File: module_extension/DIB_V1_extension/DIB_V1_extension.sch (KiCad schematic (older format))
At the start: 12 parts, among them J1 20-pin power socket, J3 28-pin module socket, J3 PROBE, J4 CABLE, J5 PROBE, J6 CABLE

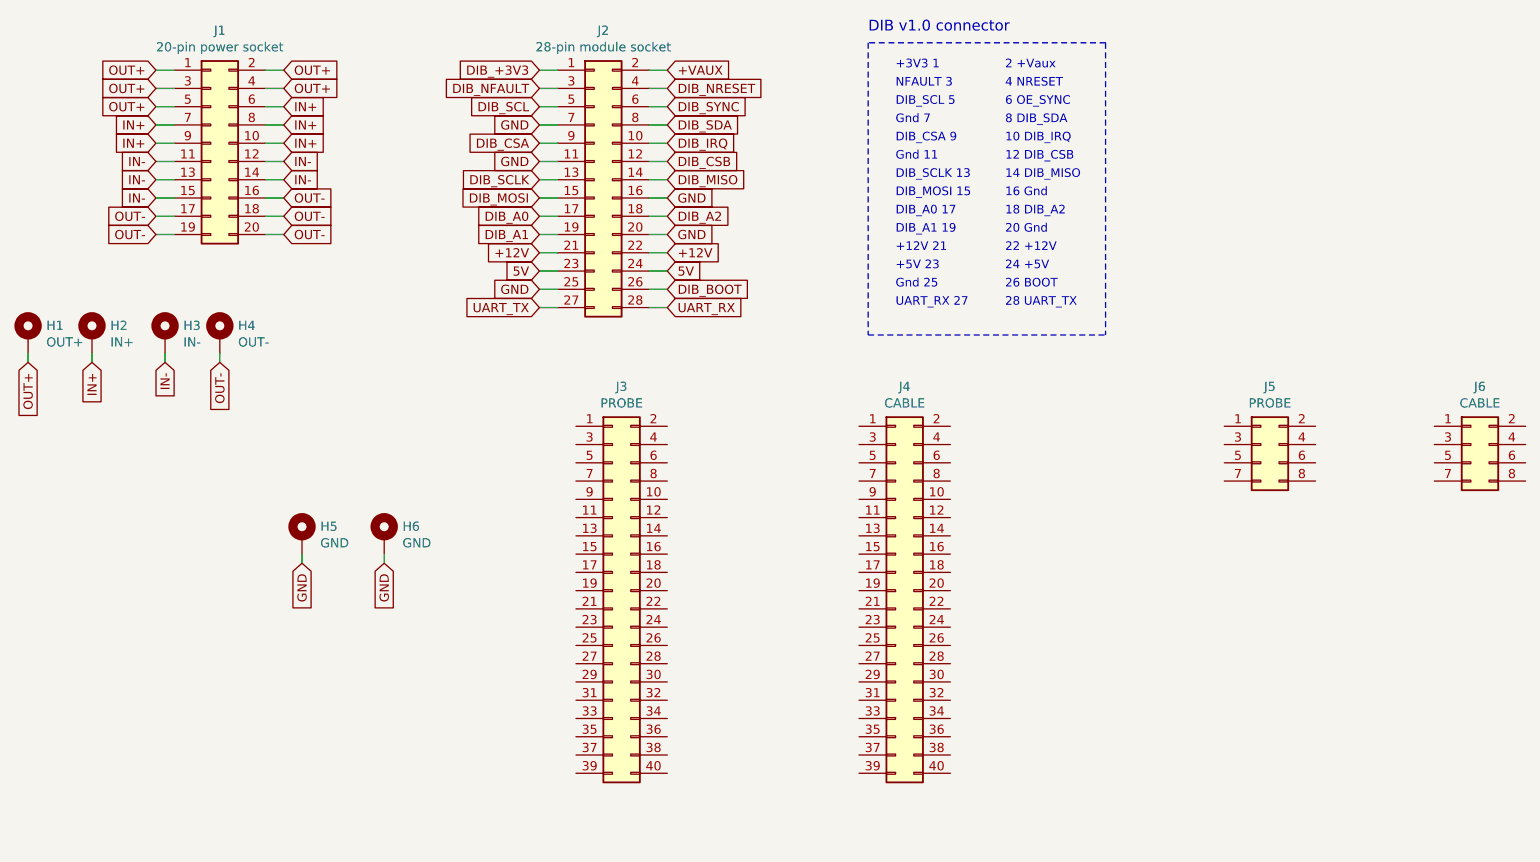
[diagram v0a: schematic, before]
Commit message: Finished routing, adding pictures and README
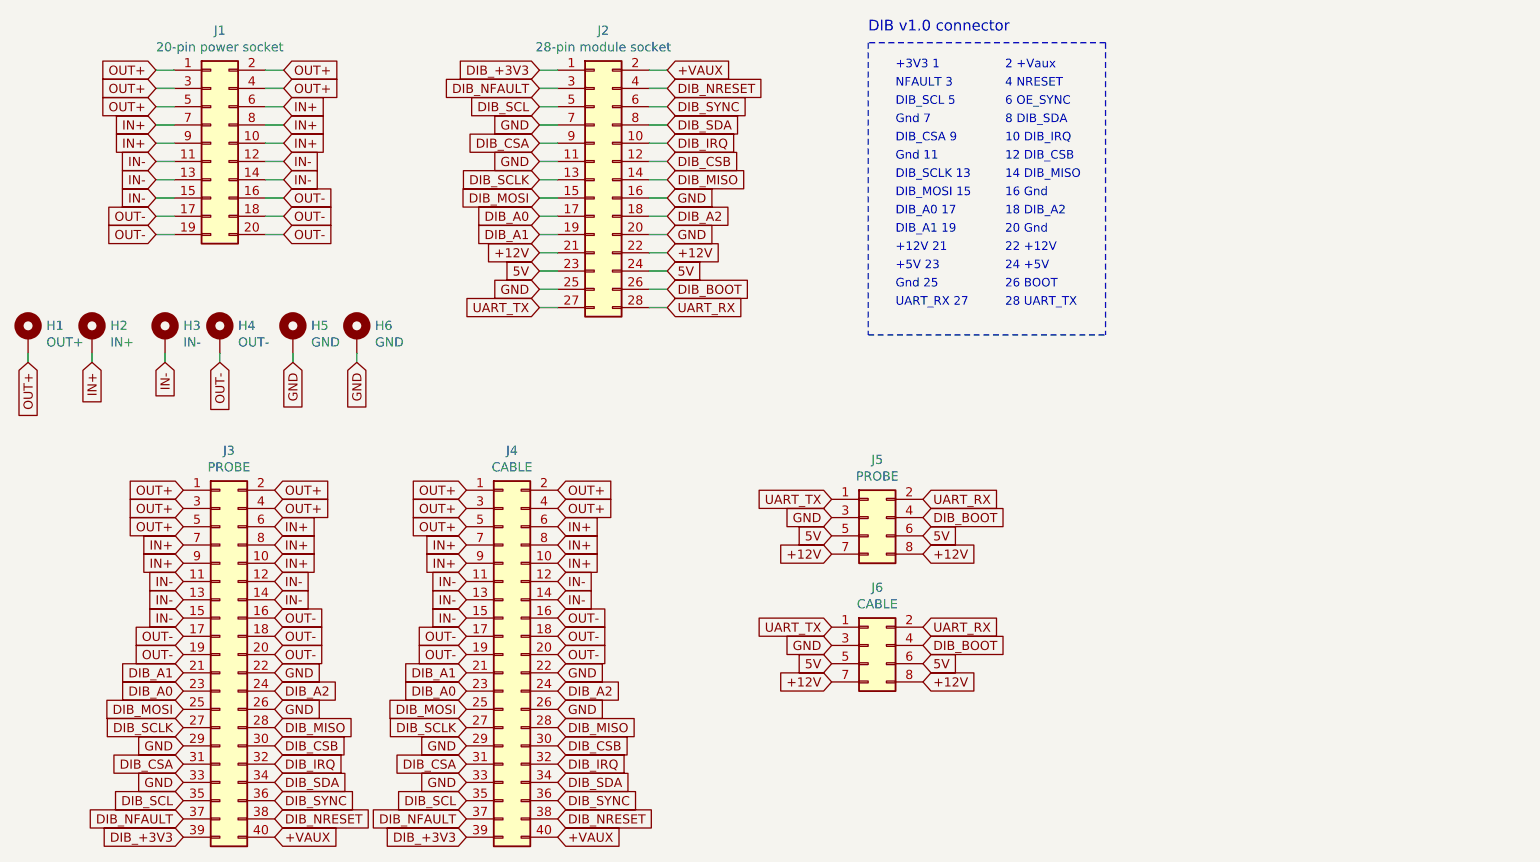
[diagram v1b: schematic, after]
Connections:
- net +12V: now also J5.7 (Pin_7), J5.8 (Pin_8), J6.7 (Pin_7), J6.8 (Pin_8)
- net +VAUX: now also J3.40 (Pin_40), J4.40 (Pin_40)
- net 5V: now also J5.5 (Pin_5), J5.6 (Pin_6), J6.5 (Pin_5), J6.6 (Pin_6)
- net DIB_+3V3: now also J3.39 (Pin_39), J4.39 (Pin_39)
- net DIB_A0: now also J3.23 (Pin_23), J4.23 (Pin_23)
- net DIB_A1: now also J3.21 (Pin_21), J4.21 (Pin_21)
- net DIB_A2: now also J3.24 (Pin_24), J4.24 (Pin_24)
- net DIB_BOOT: now also J5.4 (Pin_4), J6.4 (Pin_4)
- net DIB_CSA: now also J3.31 (Pin_31), J4.31 (Pin_31)
- net DIB_CSB: now also J3.30 (Pin_30), J4.30 (Pin_30)
- net DIB_IRQ: now also J3.32 (Pin_32), J4.32 (Pin_32)
- net DIB_MISO: now also J3.28 (Pin_28), J4.28 (Pin_28)
- net DIB_MOSI: now also J3.25 (Pin_25), J4.25 (Pin_25)
- net DIB_NFAULT: now also J3.37 (Pin_37), J4.37 (Pin_37)
- net DIB_NRESET: now also J3.38 (Pin_38), J4.38 (Pin_38)
- net DIB_SCL: now also J3.35 (Pin_35), J4.35 (Pin_35)
- net DIB_SCLK: now also J3.27 (Pin_27), J4.27 (Pin_27)
- net DIB_SDA: now also J3.34 (Pin_34), J4.34 (Pin_34)
- net DIB_SYNC: now also J3.36 (Pin_36), J4.36 (Pin_36)
- net GND: now also J3.22 (Pin_22), J3.26 (Pin_26), J3.29 (Pin_29), J3.33 (Pin_33), J4.22 (Pin_22), J4.26 (Pin_26), J4.29 (Pin_29), J4.33 (Pin_33), J5.3 (Pin_3), J6.3 (Pin_3)
- net IN+: now also J3.10 (Pin_10), J3.6 (Pin_6), J3.7 (Pin_7), J3.8 (Pin_8), J3.9 (Pin_9), J4.10 (Pin_10), J4.6 (Pin_6), J4.7 (Pin_7), J4.8 (Pin_8), J4.9 (Pin_9)
- net IN-: now also J3.11 (Pin_11), J3.12 (Pin_12), J3.13 (Pin_13), J3.14 (Pin_14), J3.15 (Pin_15), J4.11 (Pin_11), J4.12 (Pin_12), J4.13 (Pin_13), J4.14 (Pin_14), J4.15 (Pin_15)
- net OUT+: now also J3.1 (Pin_1), J3.2 (Pin_2), J3.3 (Pin_3), J3.4 (Pin_4), J3.5 (Pin_5), J4.1 (Pin_1), J4.2 (Pin_2), J4.3 (Pin_3), J4.4 (Pin_4), J4.5 (Pin_5)
- net OUT-: now also J3.16 (Pin_16), J3.17 (Pin_17), J3.18 (Pin_18), J3.19 (Pin_19), J3.20 (Pin_20), J4.16 (Pin_16), J4.17 (Pin_17), J4.18 (Pin_18), J4.19 (Pin_19), J4.20 (Pin_20)
- net UART_RX: now also J5.2 (Pin_2), J6.2 (Pin_2)
- net UART_TX: now also J5.1 (Pin_1), J6.1 (Pin_1)
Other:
- moved on the sheet: H5, H6, J3, J4, J5, J6
